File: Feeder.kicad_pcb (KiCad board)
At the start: 4 copper layers, 91 x 85 mm, 107 parts, among them J101 Conn_02x03_Odd_Even, J102 Conn_01x03_Pin, J103 Conn_01x02_Pin, U101 XBLW 24C02S(XBLW), U201 CMP6793RE, U301 CMP6793RE, U601 TPS562202, U701 TPS562202

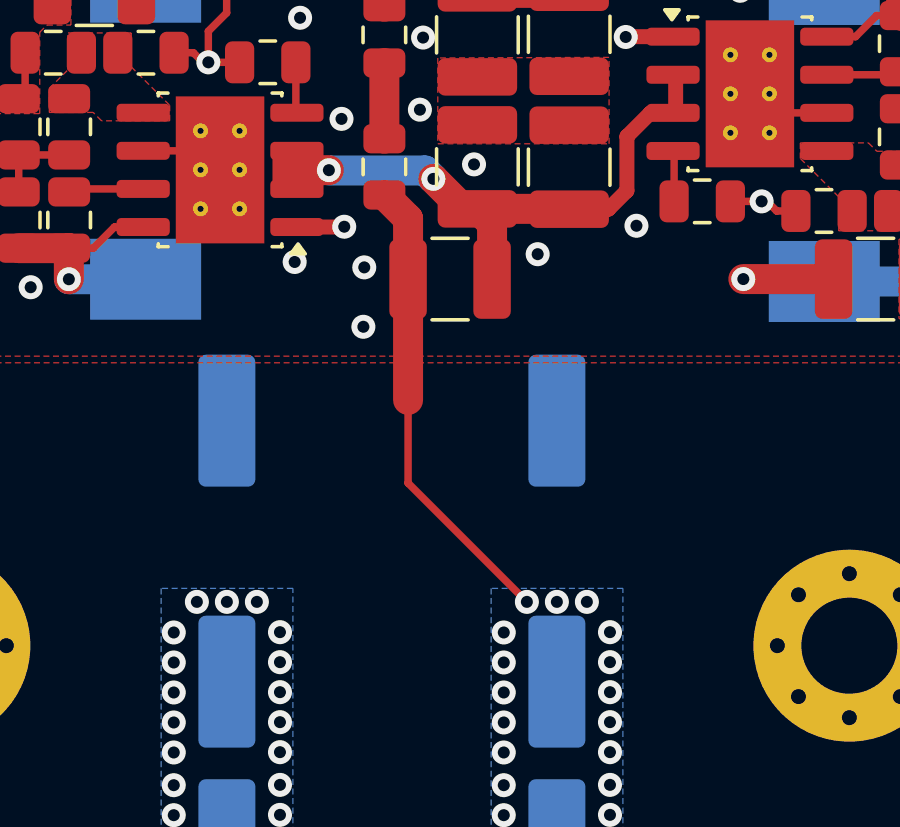
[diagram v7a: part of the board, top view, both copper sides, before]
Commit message: added drawing to the schematic
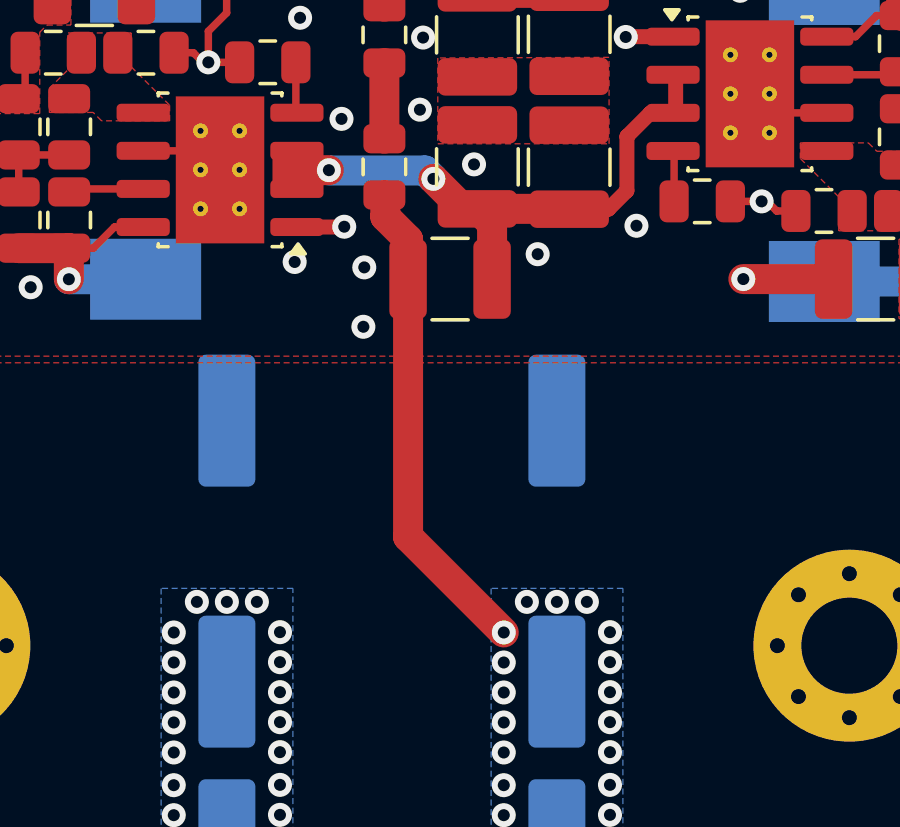
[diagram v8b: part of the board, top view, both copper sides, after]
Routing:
- net /VHigh: track 15.5 -> 16.2 mm
